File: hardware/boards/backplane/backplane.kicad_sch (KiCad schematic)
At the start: 6 parts, among them J14 DC_IN

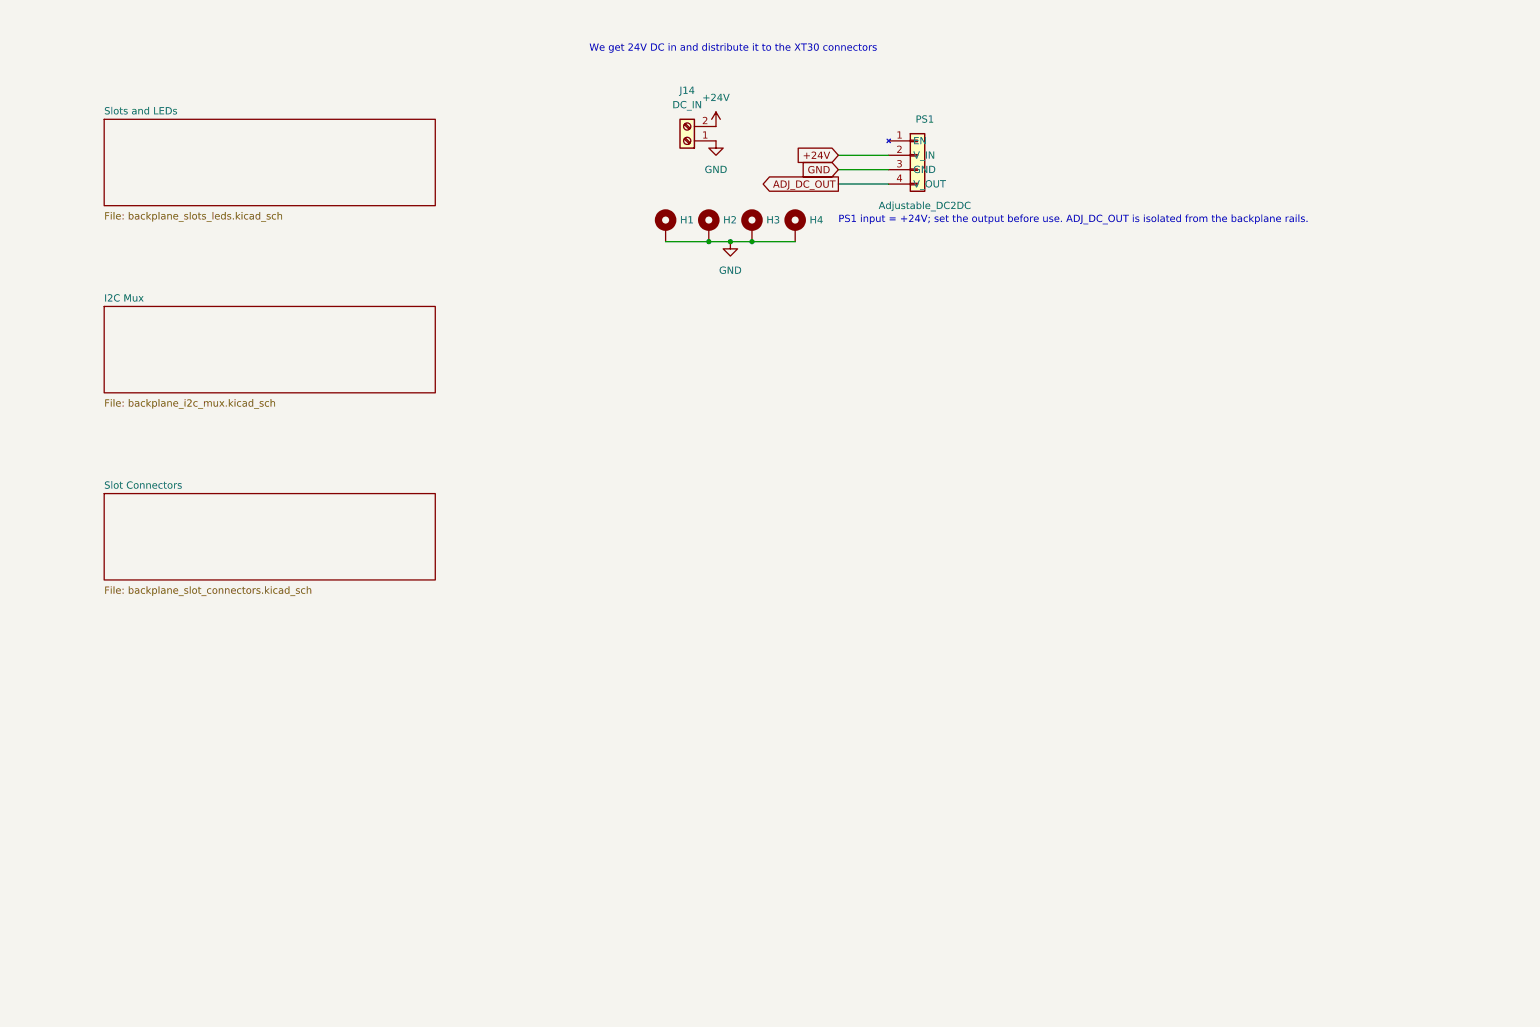
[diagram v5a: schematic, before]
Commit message: refactor: consolidate active KiCad projects under backplane and carrier
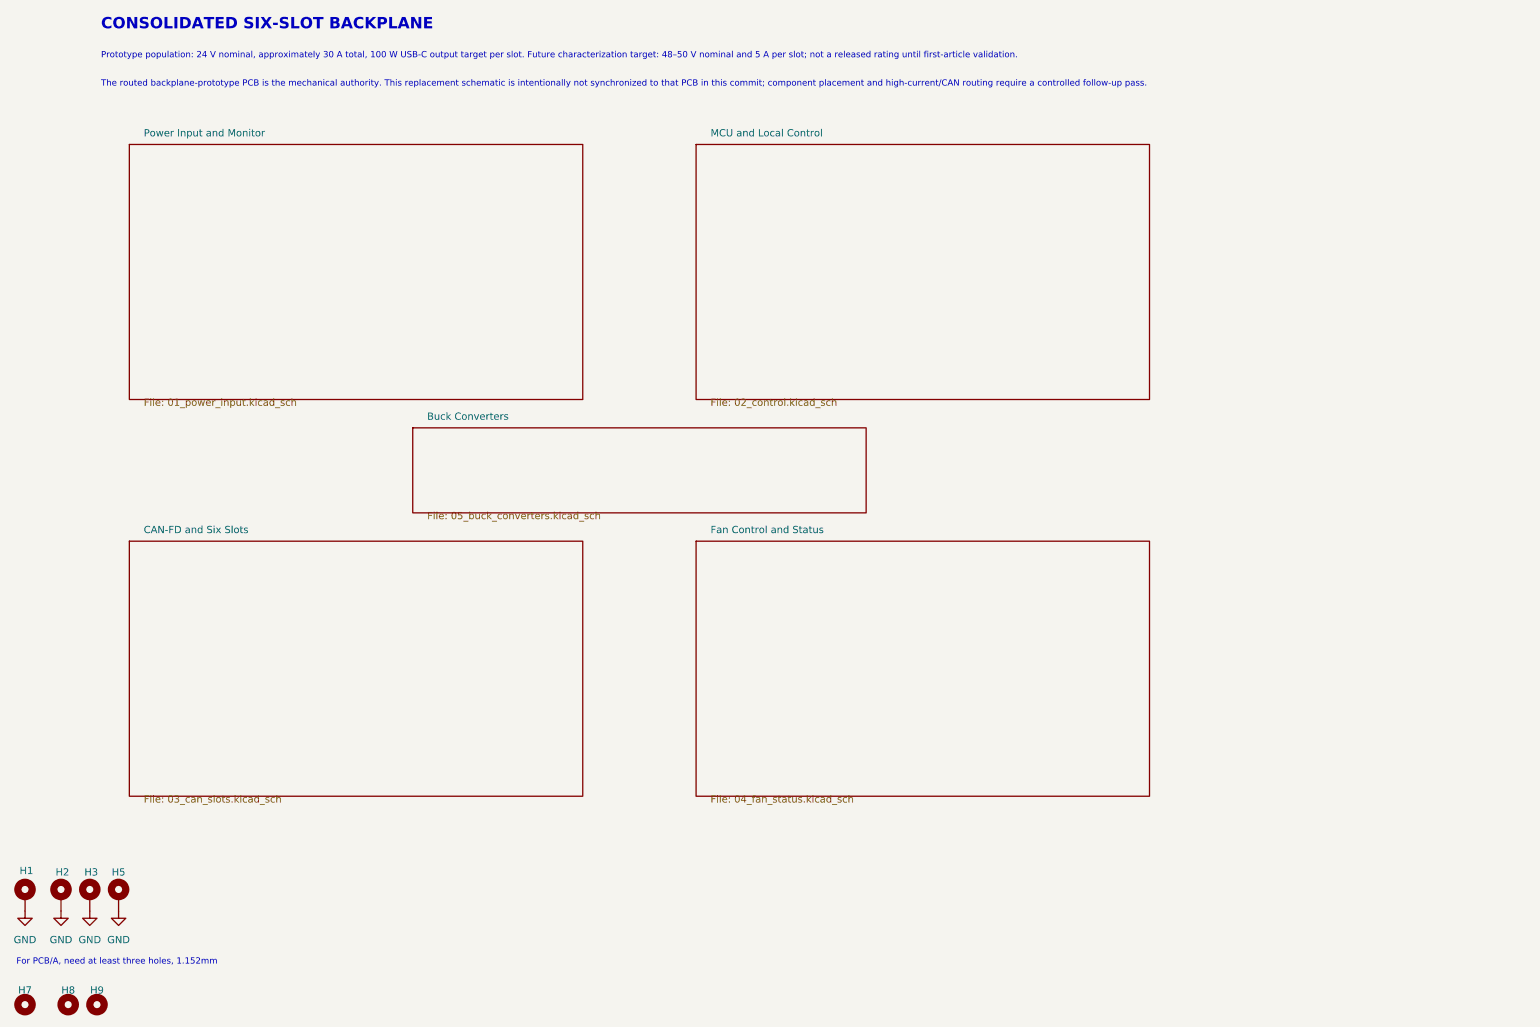
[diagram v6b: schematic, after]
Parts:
- removed H4: MountingHole_Pad, MountingHole:MountingHole_3.2mm_M3_Pad_Via, symbol Mechanical:MountingHole_Pad
- removed J14: DC_IN, mini-rack-power:DEGSON_DG135T-10.16-02P, symbol Connector:Screw_Terminal_01x02
- removed PS1: Adjustable_DC2DC, mini-rack-power:Adjustable_DC2DC, symbol mini-rack-power:Adjustable_DC2DC
- added H5: M2 CHASSIS, mini-rack-power:MountingHole_2.2mm_M2_Pad_Via_JLC, symbol Mechanical:MountingHole_Pad
- added H7, H8, H9: ToolingHole_1.152mm, mini-rack-power:MountingHole_JLCPCB_Tooling_1.152mm, symbol Mechanical:MountingHole
- H1, H2, H3: value MountingHole_Pad -> M2 CHASSIS; footprint MountingHole:MountingHole_3.2mm_M3_Pad_Via -> mini-rack-power:MountingHole_2.2mm_M2_Pad_Via_JLC
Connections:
- net GND: now also H5.1
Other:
- removed sheet I2C Mux
- removed sheet Slot Connectors
- removed sheet Slots and LEDs
- added sheet Buck Converters (05_buck_converters.kicad_sch)
- added sheet CAN-FD and Six Slots (03_can_slots.kicad_sch)
- added sheet Fan Control and Status (04_fan_status.kicad_sch)
- added sheet MCU and Local Control (02_control.kicad_sch)
- added sheet Power Input and Monitor (01_power_input.kicad_sch)
- note added: "CONSOLIDATED SIX-SLOT BACKPLANE"
- note added: "For PCB/A, need at least three holes, 1.152mm"
- note added: "Prototype population: 24 V nominal, approximately 30 A total, 100 W USB-C output target per slot. Future characterization target: 48–50 V nominal and 5 A per slot; not a released rating until first-article validation."
- note added: "The routed backplane-prototype PCB is the mechanical authority. This replacement schematic is intentionally not synchronized to that PCB in this commit; component placement and high-current/CAN routing require a controlled follow-up pass."
- note removed: "PS1 input = +24V; set the output before use. ADJ_DC_OUT is isolated from the backplane rails."
- note removed: "We get 24V DC in and distribute it to the XT30 connectors"
- title: Mini Rack Power Backplane -> (none)
